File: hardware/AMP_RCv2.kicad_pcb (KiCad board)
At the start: 2 copper layers, 100 x 85 mm, 46 parts, among them J1 USB_C_Receptacle_USB2.0_16P, SW1 SW_UP, SW2 SW_LEFT, SW3 SW_DOWN, SW4 SW_RIGHT, SW5 ON/OFF, U1 TPS61023, U2 MCP73831-2-OT, U3 JOYSTICK_LEFT, U4 JOYSTICK_RIGHT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

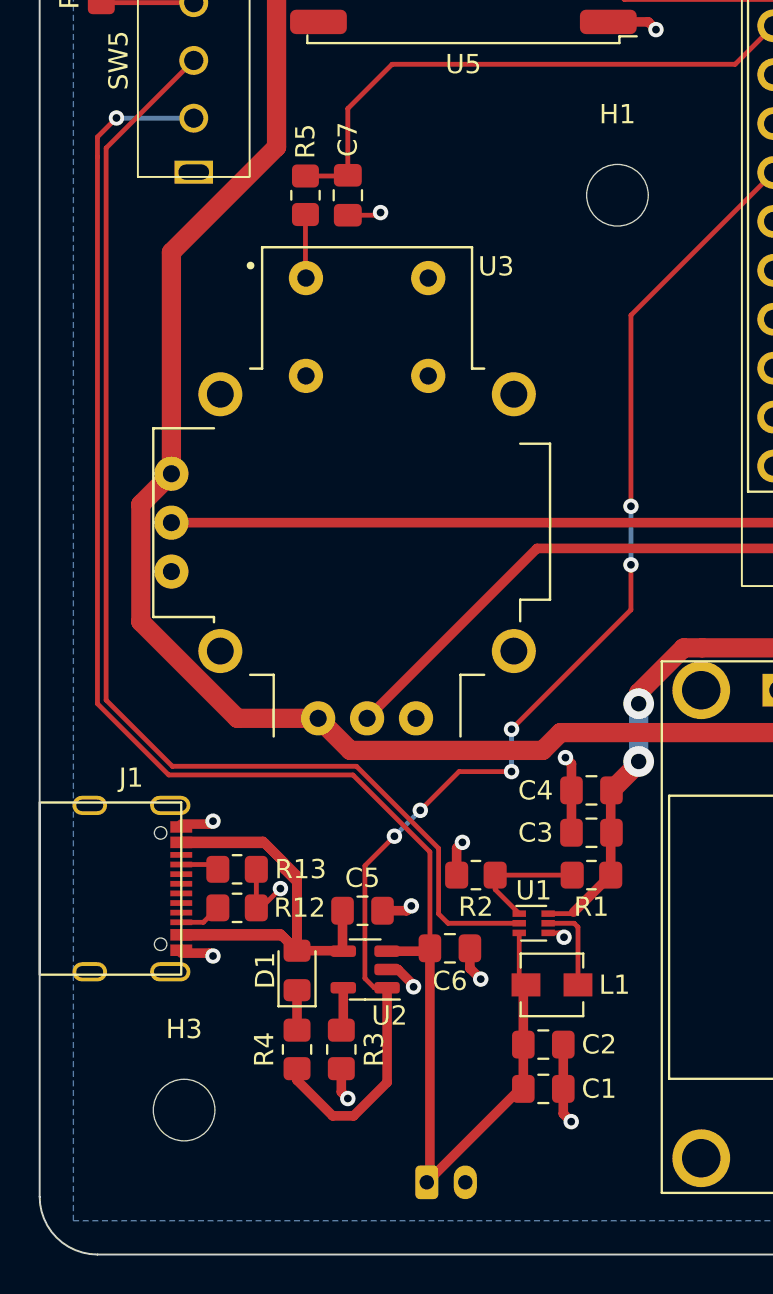
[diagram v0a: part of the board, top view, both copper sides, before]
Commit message: Replace boost converter
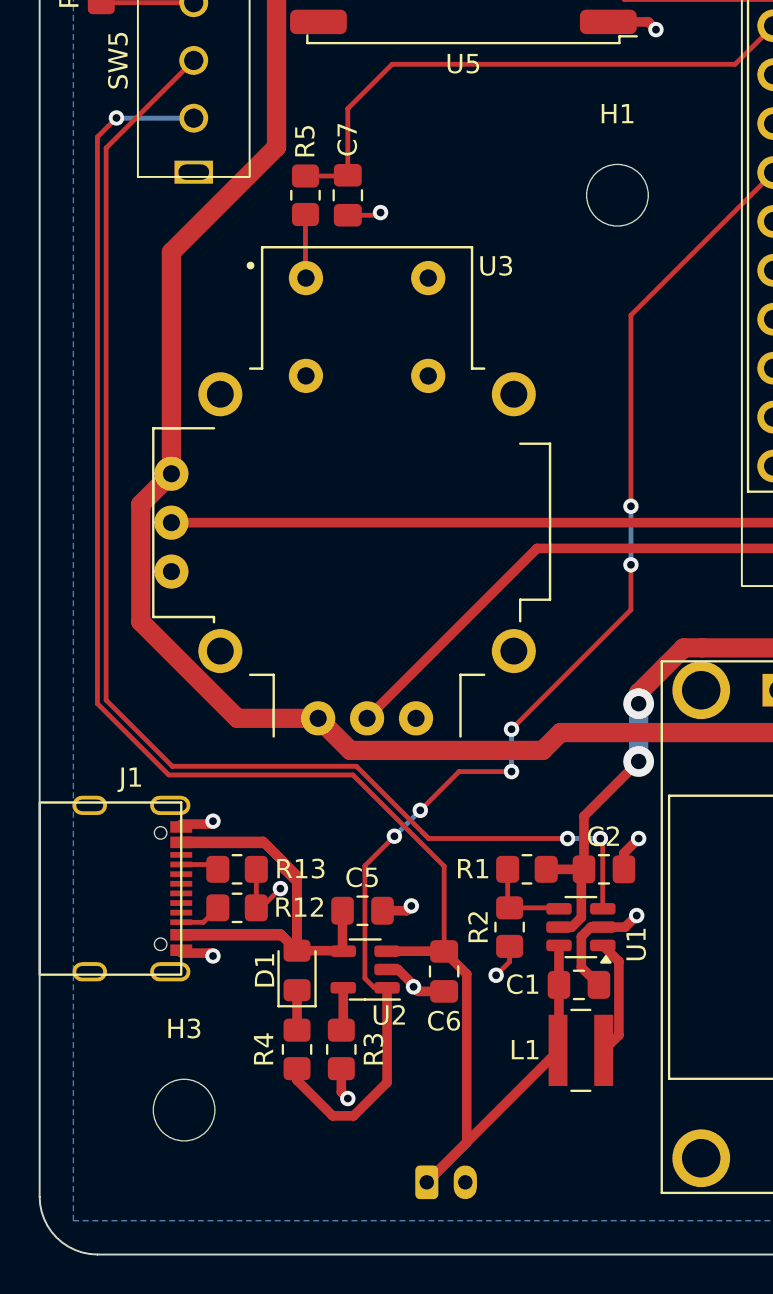
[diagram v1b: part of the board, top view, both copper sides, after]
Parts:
- removed C3, C4: 10uF, Capacitor_SMD:C_0805_2012Metric_Pad1.18x1.45mm_HandSolder
- L1: footprint Inductor_SMD:L_Vishay_IHLP-1212 -> Inductor_SMD:L_Wuerth_MAPI-4030
- R1: value 732K -> 180K
- R2: value 100K -> 20K
- U1: value TPS61023 -> TLV61070ADB; footprint Package_TO_SOT_SMD:SOT-563 -> Package_TO_SOT_SMD:SOT-23-6
- moved C2 9.63 mm to (129.3, 115.0)
- moved C1 5.71 mm to (128.0, 121.0)
- moved L1 3.72 mm to (128.1, 124.4)
- moved R1 3.36 mm to (125.3, 115.0)
- moved R2 3.22 mm to (124.4, 118.0), turned to -90 degrees
- moved U1 2.46 mm to (128.1, 118.0), turned to 180 degrees
- moved C6 1.24 mm to (121.0, 120.3), turned to -90 degrees
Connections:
- C2 pad 1: /VBAT -> +5V
- U1 pad 1: Net-(U1-FB) -> Net-(U1-SW)
- U1 pad 2: Net-(SW5-B) -> GND
- U1 pad 3: /VBAT -> Net-(SW5-B)
- U1 pad 4: GND -> Net-(U1-FB)
- U1 pad 5: Net-(U1-SW) -> +5V
- U1 pad 6: +5V -> /VBAT
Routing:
- net Net-(SW5-B): track 63.3 -> 67.4 mm, vias 0 -> 2
- net +5V: track 66.7 -> 68.9 mm
- net /VBAT: track 90.1 -> 92.2 mm
- net Net-(U1-FB): track 6.52 -> 4.62 mm
- net Net-(U1-SW): track 4.63 -> 6.12 mm
- net GND: track 44.8 -> 43.7 mm, vias 21 -> 19

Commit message: Clean up schematic and add optional second battery connector
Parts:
- added BT2: Li-ion, Connector_JST:JST_PH_B2B-PH-K_1x02_P2.00mm_Vertical, B.Cu at (114.9, 131.3)
- U6: value SSD1306 -> NUCLEO32-F303K8; footprint AMP_Custom:SSD1306_SPI -> AMP_Custom:NUCLEO32
- U7: value NUCLEO32-F303K8 -> SSD1306; footprint AMP_Custom:NUCLEO32 -> AMP_Custom:SSD1306_SPI
- moved U6 29.4 mm to (145.7, 76.3)
- moved U7 29.4 mm to (146.0, 105.7)
- moved BT1 4.00 mm to (124.1, 131.3)
- turned AE1 to 0 degrees
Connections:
- U5 pad 14: /LORA_DIO0 -> /Nucleo/LORA_DIO0
- U5 pad 2: /SPI1_MISO -> /Nucleo/SPI1_MISO
- U5 pad 3: /SPI1_MOSI -> /Nucleo/SPI1_MOSI
- U5 pad 4: /SPI1_SCK -> /Nucleo/SPI1_SCK
- U5 pad 5: /LORA_NSS -> /Nucleo/LORA_NSS
- U5 pad 6: /LORA_RST -> /Nucleo/LORA_RST
- U6 pad 1: GND -> /Nucleo/LORA_RST
- U6 pad 2: +3V3 -> /Nucleo/LORA_NSS
- U6 pad 3: /SPI1_SCK -> unconnected-(U6-NRST-Pad28)
- U6 pad 4: /SPI1_MOSI -> GND
- U6 pad 5: /OLED_RST -> /Nucleo/LORA_DIO0
- U6 pad 6: /OLED_DC -> /JOYSTICK_LEFT_SW
- U6 pad 7: /OLED_NSS -> /BUTTON_UP
- U7 pad 1: /LORA_RST -> GND
- U7 pad 2: /LORA_NSS -> +3V3
- U7 pad 3: unconnected-(U7-NRST-Pad28) -> /Nucleo/SPI1_SCK
- U7 pad 4: GND -> /Nucleo/SPI1_MOSI
- U7 pad 5: /LORA_DIO0 -> /Nucleo/OLED_RST
- U7 pad 6: /JOYSTICK_LEFT_SW -> /Nucleo/OLED_DC
- U7 pad 7: /BUTTON_UP -> /Nucleo/OLED_NSS
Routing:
- net /SPI1_SCK: track 68.7 -> 0.00 mm, vias 3 -> 0
- net /Nucleo/SPI1_SCK: track 0.00 -> 68.7 mm, vias 0 -> 3
- net /SPI1_MOSI: track 64.4 -> 0.00 mm, vias 5 -> 0
- net /Nucleo/SPI1_MOSI: track 0.00 -> 64.4 mm, vias 0 -> 5
- net /SPI1_MISO: track 25.8 -> 0.00 mm, vias 2 -> 0
- net /Nucleo/SPI1_MISO: track 0.00 -> 25.8 mm, vias 0 -> 2
- net /Nucleo/LORA_DIO0: track 0.00 -> 24.3 mm
- net /LORA_DIO0: track 24.3 -> 0.00 mm
- net /OLED_NSS: track 24.0 -> 0.00 mm, vias 2 -> 0
- net /Nucleo/OLED_NSS: track 0.00 -> 24.0 mm, vias 0 -> 2
- net /OLED_DC: track 20.1 -> 0.00 mm, vias 2 -> 0
- net /Nucleo/OLED_DC: track 0.00 -> 20.1 mm, vias 0 -> 2
- net /OLED_RST: track 16.2 -> 0.00 mm, vias 2 -> 0
- net /Nucleo/OLED_RST: track 0.00 -> 16.2 mm, vias 0 -> 2
- net /Nucleo/LORA_RST: track 0.00 -> 9.62 mm
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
